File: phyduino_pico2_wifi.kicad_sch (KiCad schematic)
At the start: 14 parts, among them U11 ESP32-C6-MINI-1, U12 TS3A24159DRC

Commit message: nigthly commit
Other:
- company: (none) -> University of Toronto, Dept. of Physics
- title: (none) -> Phyduino Pico 2
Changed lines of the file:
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@@
 	(generator_version "10.0")
 	(paper "B")
+	(title_block
+		(title "Phyduino Pico 2")
+		(date "2026-05-04")
+		(rev "A")
+		(company "University of Toronto, Dept. of Physics")
+	)
 	(rectangle
 		(start 41.91 88.9)

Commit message: Made schematic changes : merged usb_pd sheet with wifi sheet. made system regulators adjustable.
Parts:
- removed C38: 0.1µF, Capacitor_SMD [KL]:C_0402_1005Metric, symbol Component - Device [KL]:C_Small
- removed TP16, TP17: TestPoint_Small, Component - Test point SMT [UL]:TestPoint_SameSky_CPG-47-TH-B, symbol Connector [KL]:TestPoint_Small
- removed U12: TS3A24159DRC, Package_SON [KL]:Texas_S-PVSON-N10, symbol Analog - Switches - Analog Devices [KL]:TS3A24159DRC
- added C131, C132: 0.1µF, Capacitor_SMD [KL]:C_0402_1005Metric, symbol Device:C_Small
- added C16, C24, C33, C35: 0.1μF, Capacitor_SMD [KL]:C_0805_2012Metric_Pad1.18x1.45mm_HandSolder, symbol Component - Device [KL]:C_Small
- added C17, C18, C25, C27, C36: 22µF, Capacitor_SMD [KL]:C_0805_2012Metric_Pad1.18x1.45mm_HandSolder, symbol Component - Device [KL]:C_Small
- added C19, C23, C29, C32: 10μF, Capacitor_SMD [KL]:C_0805_2012Metric_Pad1.18x1.45mm_HandSolder, symbol Component - Device [KL]:C_Small
- added C28, C9: 0.1µF, Capacitor_SMD [KL]:C_1206_3216Metric_Pad1.33x1.80mm_HandSolder, symbol Component - Device [KL]:C_Small
- added C30: 1µF, Capacitor_SMD [KL]:C_0402_1005Metric, symbol Component - Device [KL]:C_Small
- added C31, C6: 0.1µF, Capacitor_SMD [KL]:C_0402_1005Metric, symbol Component - Device [KL]:C_Small
- added C5, C7: 100pF, Capacitor_SMD [KL]:C_0805_2012Metric_Pad1.18x1.45mm_HandSolder, symbol Component - Device [KL]:C_Small
- added J6, J9: GT-USB-7047A, Connector - PC SMT [UL]:GCT-USBC-GCT_USB4110, symbol KL - Connector:USB_C_Receptacle_USB2.0_16P
- added L1: 6.8µH, Component - Inductor SMT [UL]:L_Bourns_SRP4021HMCT, symbol Inductor - Bourns:L_Bourns_SRP4021HMCT-3R3M
- added L2: 10µH, Component - Inductor SMT [UL]:L_Bourns_SRP4021HMCT, symbol Inductor - Bourns:L_Bourns_SRP4021HMCT-4R7M
- added Q1, Q2: SP30P25NQ, Package_DFN_QFN [KL]:Diodes_UDFN2020-6_Type-F, symbol UL - Transistors - MOSFET:PMPB27EP
- added R10: 5mΩ, Resistor_SMD [KL]:R_0603_1608Metric, symbol Component - Device [KL]:R_Small
- added R11, R12, R7, R8: 5.1kΩ, Resistor_SMD [KL]:R_0402_1005Metric, symbol Component - Device [KL]:R_Small
- added R134: 42.2kΩ, Resistor_SMD [KL]:R_0402_1005Metric, symbol Device:R_Small
- added R135, R138: 21kΩ, Resistor_SMD [KL]:R_0402_1005Metric, symbol Device:R_Small
- added R136, R137: 5.1kΩ, Resistor_SMD [KL]:R_0402_1005Metric, symbol Device:R_Small
- added R139, R141: 154kΩ, Resistor_SMD [KL]:R_0402_1005Metric, symbol Device:R_Small
- added R140, R143, R144: 39.2kΩ, Resistor_SMD [KL]:R_0402_1005Metric, symbol Device:R_Small
- added R142, R145: 10kΩ, Resistor_SMD [KL]:R_0402_1005Metric, symbol Device:R_Small
- added R37, R47, R48: 5.1kΩ, Resistor_SMD [KL]:R_0402_1005Metric, symbol phyduino_pico:R_Small
- added R40, R41: 100Ω, Resistor_SMD [KL]:R_0402_1005Metric, symbol phyduino_pico:R_Small
- added R51: 47kΩ, Resistor_SMD [KL]:R_0805_2012Metric_Pad1.20x1.40mm_HandSolder, symbol phyduino_pico:R_Small
- added R52: 16.5kΩ, Resistor_SMD [KL]:R_0805_2012Metric_Pad1.20x1.40mm_HandSolder, symbol phyduino_pico:R_Small
- added R53: 111kΩ, Resistor_SMD [KL]:R_0805_2012Metric_Pad1.20x1.40mm_HandSolder, symbol phyduino_pico:R_Small
- added R54: 18.7kΩ, Resistor_SMD [KL]:R_0805_2012Metric_Pad1.20x1.40mm_HandSolder, symbol phyduino_pico:R_Small
- added R56: 196kΩ, Resistor_SMD [KL]:R_0805_2012Metric_Pad1.20x1.40mm_HandSolder, symbol phyduino_pico:R_Small
- added R57: 62kΩ, Resistor_SMD [KL]:R_0805_2012Metric_Pad1.20x1.40mm_HandSolder, symbol phyduino_pico:R_Small
- added R58: 157kΩ, Resistor_SMD [KL]:R_0805_2012Metric_Pad1.20x1.40mm_HandSolder, symbol phyduino_pico:R_Small
- added R59: 30kΩ, Resistor_SMD [KL]:R_0805_2012Metric_Pad1.20x1.40mm_HandSolder, symbol phyduino_pico:R_Small
- added R6, R9: 220kΩ, Resistor_SMD [KL]:R_0805_2012Metric_Pad1.20x1.40mm_HandSolder, symbol Component - Device [KL]:R_Small
- added TH1: 10kΩ@25°C, Resistor_SMD [KL]:R_0402_1005Metric, symbol Component - Device [KL]:Thermistor_NTC
- added TP10, TP11, TP13, TP18, TP2, TP22, TP4, TP5, TP6, TP7: TestPoint_Small, Component - Test point SMT [UL]:TestPoint_SameSky_CPG-47-TH-B, symbol Connector [KL]:TestPoint_Small
- added U10, U8: AP63200WU, Package_TO_SOT_SMD [KL]:TSOT-23-6_HandSoldering, symbol Power - Switching Regulator [KL]:AP63200WU
- added U108, U109: TPS2121RUXR, Package - QFN [UL]:VQFN-HR-12, symbol PMIC - TI:TPS2121RUX
- added U6: AP33772SDKZ-13-FA02, Package_DFN_QFN [KL]:QFN-24-1EP_4x4mm_P0.5mm_EP2.75x2.75mm, symbol Interface - USB:AP33772S
- added U9: TPUSBLC6-2P6, Package_TO_SOT_SMD [KL]:SOT-666, symbol Protection - Signal:USBLC6-2P6
- added Z3: ESDA25P35-1U1M-ES, Diode_SMD [KL]:ST_QFN-2L_1.6x1.0mm, symbol phyduino_pico:D_Zener_Filled
- U11: value ESP32-C6-MINI-1 -> ESP32-C6-MINI-1-H4
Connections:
- net WIFI_UART_RX is gone; now on net WIFI_DL_UART_RX: TP9.1
- net WIFI_UART_TX is gone; now on net WIFI_DL_UART_TX: TP8.1
- net +3.3V: now also C17.1, C18.1, C5.1, L1.2, R56.1, R7.1, R8.1, U9.5 (VBUS)
- net GND: now also C131.2, C132.2, C17.2, C18.2, C19.2, C23.2, C25.2, C27.2, C28.2, C29.2, C30.1, C31.1, C32.2, C33.2, C35.2, C36.2, C6.1, C9.2, J6.A1 (GND), J6.A12 (GND), J6.B1 (GND), J6.B12 (GND), J9.A1 (GND), J9.A12 (GND), J9.B1 (GND), J9.B12 (GND), R11.2, R12.2, R134.1, R136.1, R137.1, R143.1, R144.1, R145.1, R47.2, R48.2, R52.2, R54.2, R57.2, R59.2, R6.2, R9.2, TH1.2, U10.4 (GND), U108.12 (GND), U108.3 (CP2), U108.6 (PR1), U108.9 (ST), U109.12 (GND), U6.25 (EP), U6.3 (GND), U8.4 (GND), U9.2 (GND), Z3.2 (A)
- net WIFI_AT_UART_CTS: now reaches U11.10 (IO5)
- net XTAL_32K_P: now reaches U11.12 (IO0)
- net XTAL_32K_N: now reaches U11.13 (IO1)
- net WIFI_AT_UART_RX: now reaches U11.15 (IO6)
- net WIFI_AT_UART_RX: now also R55.2
- net WIFI_AT_UART_TX: now reaches U11.16 (IO7)
- net WIFI_AT_UART_RTS: now reaches U11.9 (IO4)
- net AT_UART_RX: no longer names the net of U11.25 (IO19)
- net AT_UART_RX: no longer R55.2
- net AT_UART_TX: no longer names the net of U11.28 (IO22)
- net DL_UART_RX renamed WIFI_DL_UART_RX
- net DL_UART_TXD renamed WIFI_DL_UART_TX
- net WIFI_UART_CTS: no longer names the net of U11.20 (IO15)
- net WIFI_UART_RTS: no longer names the net of U11.19 (IO14)
- new net: J9.A6 (D+), J9.B6 (D+)
- new net: J9.A7 (D-), J9.B7 (D-)
- new net: R40.1, R41.2
- new net: U6.10 (NC), U6.14 (NC), U6.2 (NC), U6.21 (NC)
- new net +5.0V: U108.1 (OUT), U108.8 (OUT)
- new net +5.0V_DCDC: C25.1, C36.1, C7.1, L2.2, R135.2, R58.1, TP22.1, U108.7 (IN1)
- new net +VUSB: C19.1, C23.1, R138.2, R51.1, R53.1, TP13.1, U10.3 (IN), U108.2 (IN2), U109.1 (OUT), U109.8 (OUT), U8.3 (IN)
- new net +VUSB_COMM: C27.1, J6.A4 (VBUS), J6.A9 (VBUS), J6.B4 (VBUS), J6.B9 (VBUS), R139.2, TP18.1, U109.7 (IN1)
- new net +VUSB_PD: C29.1, C33.1, J9.A4 (VBUS), J9.A9 (VBUS), J9.B4 (VBUS), J9.B9 (VBUS), R10.1, U6.1 (ISENP), Z3.1 (K)
- new net +VUSB_PD_OUT: C32.1, C35.1, Q2.1 (D), Q2.2 (D), Q2.5 (D), Q2.6 (D), Q2.7 (D), R141.2, R41.1, TP11.1, U109.2 (IN2)
- new net DCDC_3V3_BST: C16.1, U8.6 (BST)
- new net DCDC_3V3_EN: R51.2, R52.1, U8.2 (EN)
- new net DCDC_3V3_FB: C5.2, R56.2, R57.1, U8.1 (FB)
- new net DCDC_3V3_SW: C16.2, L1.1, U8.5 (SW)
- new net DCDC_5V0_BST: C24.1, U10.6 (BST)
- new net DCDC_5V0_EN: R53.2, R54.1, U10.2 (EN)
- new net DCDC_5V0_FB: C7.2, R58.2, R59.1, U10.1 (FB)
- new net DCDC_5V0_SW: C24.2, L2.1, U10.5 (SW)
- new net I2C1_SCL: R7.2, U6.5 (SCL)
- new net I2C1_SDA: R8.2, U6.4 (SDA)
- new net PMUX_LIM: R134.2, U108.10 (ILM)
- new net PMUX_OV1: R135.1, R136.2, U108.5 (OV1)
- new net PMUX_OV2: R137.2, R138.1, U108.4 (OV2)
- new net PMUX_SS: C131.1, U108.11 (SS)
- new net PSW_STATUS: U109.9 (ST)
- new net USBPD_CC1: J9.A5 (CC1), R11.1, TP4.1, U6.17 (CC1)
- new net USBPD_CC2: J9.B5 (CC2), R12.1, TP6.1, U6.16 (CC2)
- new net USBPD_FLIP: U6.6 (FLIP)
- new net USBPD_GPIO: U6.7 (GPIO)
- new net USBPD_IFB: C31.2, U6.15 (IFB)
- new net USBPD_INT: U6.9 (INT)
- new net USBPD_OTP: TH1.1, U6.13 (OTP)
- new net USBPD_PROT_GATE: Q1.3 (G), Q2.3 (G), R37.1
- new net USBPD_PROT_SOURCE_DRAIN: Q1.4 (S), Q1.8 (S), Q2.4 (S), Q2.8 (S), TP5.1
- new net USBPD_PWR_EN: R37.2, TP10.1, U6.23 (PWR_EN)
- new net USBPD_V18: C6.2, U6.12 (V18)
- new net USBPD_V5V: C30.2, U6.20 (V5V)
- new net USBPD_VCC: Q1.1 (D), Q1.2 (D), Q1.5 (D), Q1.6 (D), Q1.7 (D), R10.2, TP2.1, U6.24 (VCC)
- new net USBPD_VOUT: R40.2, TP7.1, U6.22 (VOUT)
- new net USB_CC1: J6.A5 (CC1), R48.1
- new net USB_CC2: J6.B5 (CC2), R47.1
- new net USB_COM_D_N: J6.A7 (D-), J6.B7 (D-), U9.4 (I/O2)
- new net USB_COM_D_P: J6.A6 (D+), J6.B6 (D+), U9.6 (I/O1)
- new net USB_COM_SHIELD: C9.1, J6.S1 (SH), R6.1
- new net USB_D_N: U9.3 (I/O2)
- new net USB_D_P: U9.1 (I/O1)
- new net USB_PD_SHIELD: C28.1, J9.S1 (SH), R9.1
- new net USB_PMUX_CP2: R141.1, R142.2, U109.3 (CP2)
- new net USB_PMUX_LIM: R143.2, U109.10 (ILM)
- new net USB_PMUX_OV1: R140.1, R145.2, U109.5 (OV1)
- new net USB_PMUX_OV2: R142.1, R144.2, U109.4 (OV2)
- new net USB_PMUX_PR1: R139.1, R140.2, U109.6 (PR1)
- new net USB_PMUX_SS: C132.1, U109.11 (SS)
- no-connect marks 14 -> 28
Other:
- note added: "- 2.4GHz Wi-Fi 6 & BLE 5.0"
- note added: "- Both modules are pin compatiable, either can be used."
- note added: "- ESP-AT version 4.1.1.0"
- note added: "- ESP-AT version 5.0.1.0"
- note added: "- GitHub fork repo for ESP-AT: https://github.com/perc-sw/esp-at"
- note added: "- Hardware connection guide : https://docs.espressif.com/projects/esp-at/en/latest/esp32c6/Get_Started/Hardware_connection.html"
- note added: "- Hardware connection guide : https://docs.espressif.com/projects/esp-at/en/latest/esp32c61/Get_Started/Hardware_connection.html"
- note added: "- J6 Only provides +5.0V (3A) power and USB 2.0 communication."
- note added: "- J9 can negoiate +5.0V to 20.0V with current ouput varying form 100mA to 5.0A"
- note added: "- Not for low power applications."
- note added: "- To download ESP-AT firmware to ESP32 module use UART0 pins (TXD0 & RXD0)."
- note added: "- U10 will only enable when +VUSB is above +7.0V."
- note added: "- U108 select between +VUSB and the output of U10. If both voltages are below +5.5V, U10's output will be selected."
- note added: "- U109 will select which input power gets used. +VUSB_PD has priority if present."
- note added: "- U8 will only enable when +VUSB is above +4.3V."
- note added: "- Using ESP-AT as the network interface API."
- note added: ">1.06V"
- note added: "ESP32-C6-MINI-1:"
- note added: "ESP32-C61-MINI-1:"
- note added: "I^{2}C Addr = 0x52"
- note added: "I_{LIMIT} = 2.6A"
- note added: "I_{LIMIT} = 2.7A"
- note added: "Low=Disable, High=Enable"
- note added: "NOTES:"
- note added: "Over Voltage Protection = 22V"
- note added: "Over Voltage Protection= 5.5V"
- note added: "Required Hardware connections"
- note added: "System Power Regulators"
- note added: "UART/USB Firmware download"
- note added: "USB Power Delivery"
- note added: "V_{EN}=4.3V"
- note added: "V_{EN}=7.0V"
- note added: "V_{OVER} = 5.5V"
- note added: "WiFi Module Interface"
- moved on the sheet: C13, C37, R44, R45, R50, R55, TP14, TP8, TP9, U11

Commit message: development update.
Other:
- moved on the sheet: C132, R139, R140, R141, R142, R143, R144, R145, TP11, TP13, TP18, U109

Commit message: Made changes to the power tree to allow +Vin to power the board.
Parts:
- removed R53: 111kΩ, Resistor_SMD [KL]:R_0805_2012Metric_Pad1.20x1.40mm_HandSolder, symbol phyduino_pico:R_Small
- removed R54: 18.7kΩ, Resistor_SMD [KL]:R_0805_2012Metric_Pad1.20x1.40mm_HandSolder, symbol phyduino_pico:R_Small
- added C134: 0.1µF, Capacitor_SMD [KL]:C_0402_1005Metric, symbol Device:C_Small
- added R146, R149: 154kΩ, Resistor_SMD [KL]:R_0402_1005Metric, symbol Device:R_Small
- added R147: 49.2kΩ, Resistor_SMD [KL]:R_0402_1005Metric, symbol Device:R_Small
- added R150, R153: 10kΩ, Resistor_SMD [KL]:R_0402_1005Metric, symbol Device:R_Small
- added R151, R152: 39.2kΩ, Resistor_SMD [KL]:R_0402_1005Metric, symbol Device:R_Small
- added TP16, TP17: TestPoint_Small, Component - Test point SMT [UL]:TestPoint_SameSky_CPG-47-TH-B, symbol Connector [KL]:TestPoint_Small
- added U110: TPS2121RUXR, Package - QFN [UL]:VQFN-HR-12, symbol PMIC - TI:TPS2121RUX
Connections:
- net PSW_STATUS is gone; now on net GND: U109.9 (ST)
- net +3.3V: now also R153.2
- net +VUSB_COMM: now also TP16.1, U110.2 (IN2); no longer TP18.1, U109.7 (IN1)
- net +VUSB_PD_OUT: now also TP18.1, U109.7 (IN1), R149.2; no longer R141.2, TP11.1, U109.2 (IN2)
- net DCDC_5V0_EN: now also U108.9 (ST), R153.1
- net GND: now also C134.2, R147.1, R151.1, R152.1, U110.12 (GND), U110.5 (OV1), U110.9 (ST); no longer U108.9 (ST)
- net +VUSB renamed +VMUX
- net +VMUX: now also TP17.1, U110.1 (OUT), U110.8 (OUT); no longer TP13.1, U109.1 (OUT), U109.8 (OUT)
- net USB_PMUX_CP2 renamed USB_PMUX1_CP2
- net USB_PMUX_LIM renamed USB_PMUX1_LIM
- net USB_PMUX_OV1 renamed USB_PMUX2_OV2
- net USB_PMUX2_OV2: now also U110.4 (OV2); no longer U109.5 (OV1)
- net USB_PMUX_OV2 renamed USB_PMUX1_OV2
- net USB_PMUX_PR1 renamed USB_PMUX2_CP2
- net USB_PMUX2_CP2: now also U110.3 (CP2); no longer U109.6 (PR1)
- net USB_PMUX_SS renamed USB_PMUX1_SS
- new net +VIN: R141.2, TP11.1, U109.2 (IN2)
- new net +VUSB_IN: R146.2, TP13.1, U109.1 (OUT), U109.8 (OUT), U110.7 (IN1)
- new net USB_PMUX1_OV1: R150.1, R151.2, U109.5 (OV1)
- new net USB_PMUX1_PR1: R149.1, R150.2, U109.6 (PR1)
- new net USB_PMUX2_LIM: R152.2, U110.10 (ILM)
- new net USB_PMUX2_PR1: R146.1, R147.2, U110.6 (PR1)
- new net USB_PMUX2_SS: C134.1, U110.11 (SS)
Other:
- note added: "- +VIN input can vary between +9.0V and +20.0V"
- note added: "Enables +5.0V DC/DC when VIN2 > 6.0V"
- note added: "ST [0b1] = IN1 ST [0b0] = IN2"
- note removed: "Over Voltage Protection = 22V"
- note removed: "Over Voltage Protection= 5.5V"
- note removed: "V_{EN}=7.0V"
- moved on the sheet: C131, C132, C16, C17, C18, C19, C23, C24, C25, C27, C28, C29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

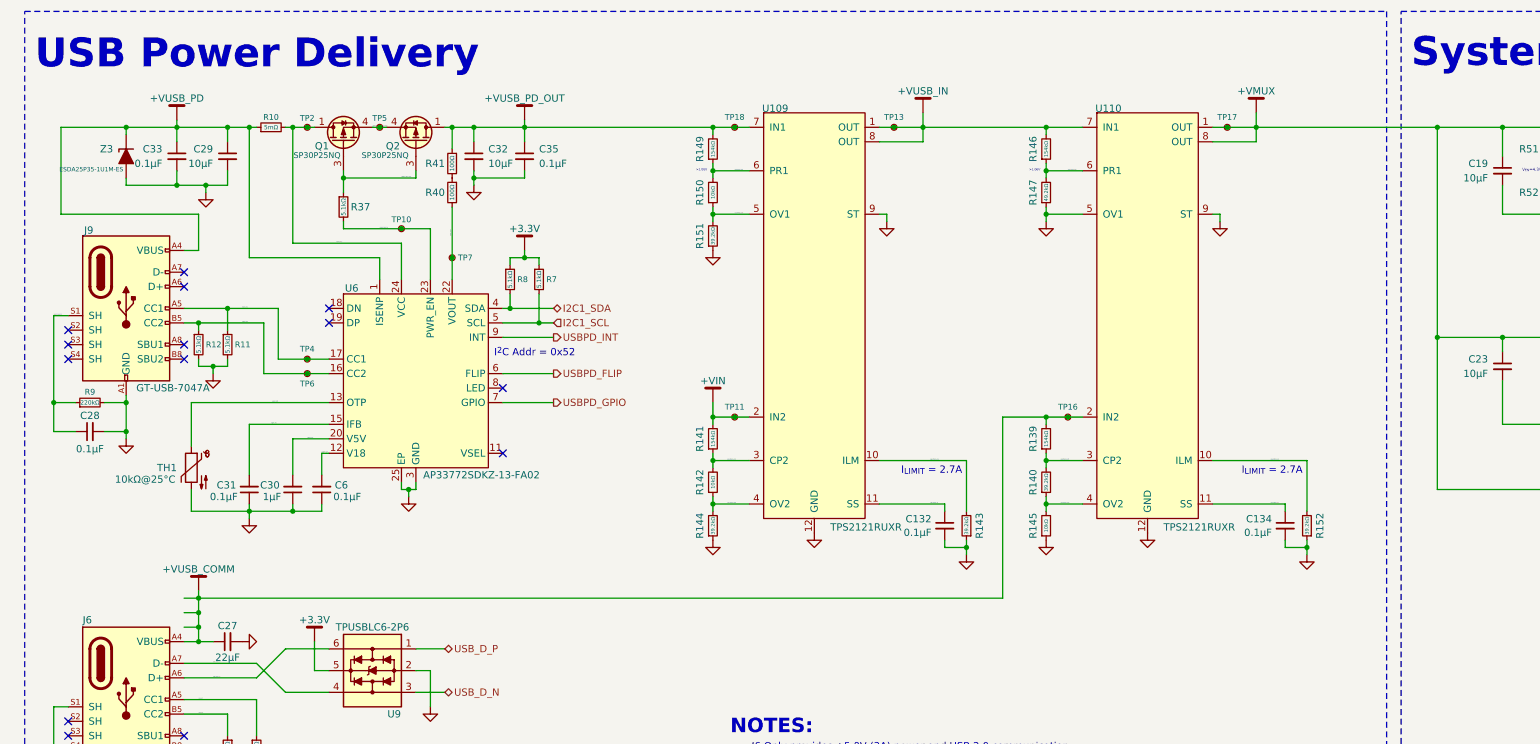
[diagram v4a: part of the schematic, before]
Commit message: Changed power tree to accept +Vin.
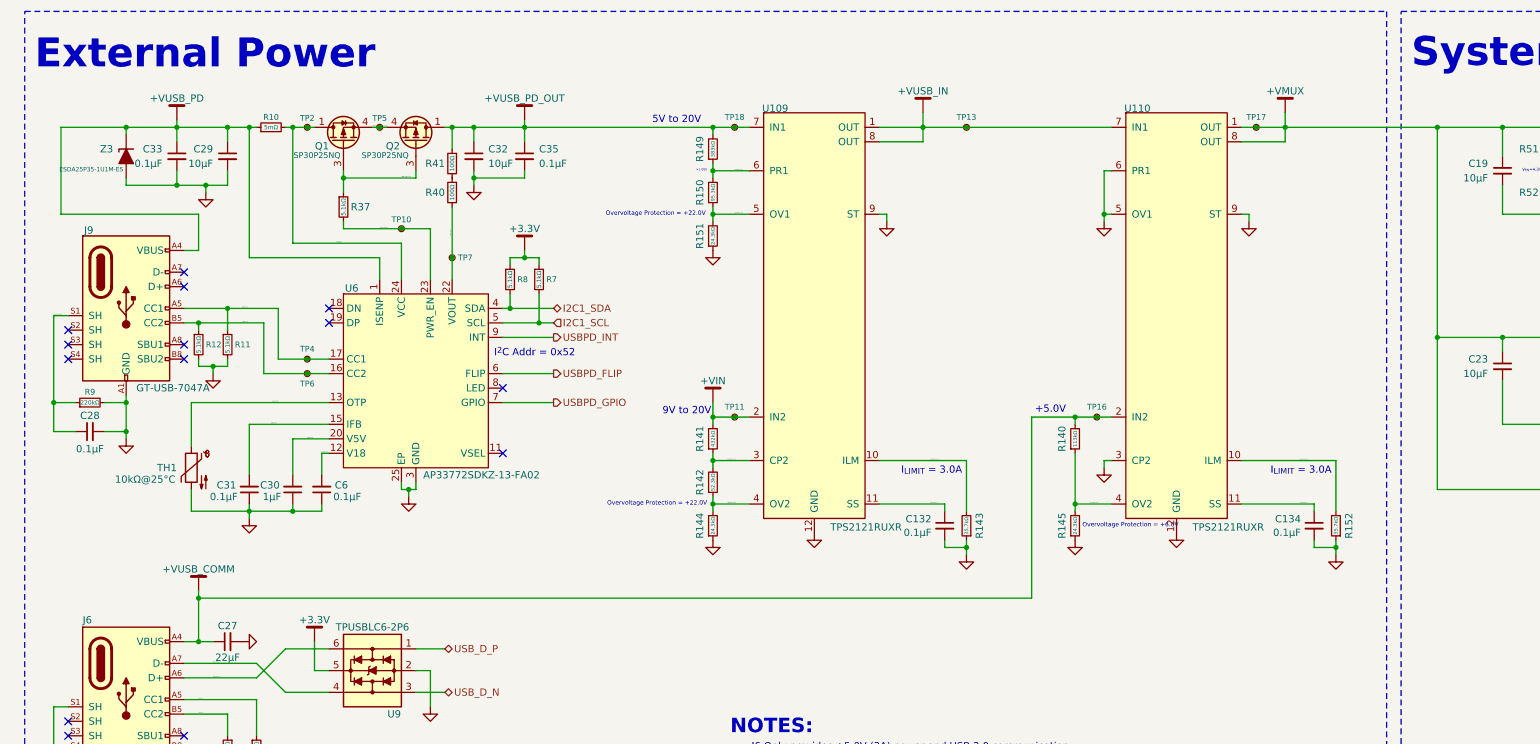
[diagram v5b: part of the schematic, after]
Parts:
- removed R139, R146: 154kΩ, Resistor_SMD [KL]:R_0402_1005Metric, symbol Device:R_Small
- removed R147: 49.2kΩ, Resistor_SMD [KL]:R_0402_1005Metric, symbol Device:R_Small
- R140: value 39.2kΩ -> 113kΩ
- R141: value 154kΩ -> 432kΩ
- R142: value 10kΩ -> 52.3kΩ
- R143, R152: value 39.2kΩ -> 35.7kΩ
- R144, R151: value 39.2kΩ -> 24.3kΩ
- R145: value 10kΩ -> 24.3kΩ
- R149: value 154kΩ -> 383kΩ
- R150: value 10kΩ -> 95.3kΩ
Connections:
- net USB_PMUX2_PR1 is gone; now on net GND: U110.6 (PR1)
- net +VUSB_COMM: now also R140.2
- net GND: now also U110.3 (CP2)
- removed net USB_PMUX2_CP2: R140.2, U110.3 (CP2)
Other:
- note added: "+5.0V"
- note added: "5V to 20V"
- note added: "9V to 20V"
- note added: "External Power"
- note added: "I_{LIMIT} = 3.0A"
- note added: "Overvoltage Protection = +22.0V"
- note added: "Overvoltage Protection = +6.0V"
- note removed: "I_{LIMIT} = 2.7A"
- note removed: "USB Power Delivery"
- moved on the sheet: C134, R140, R145, R152, TP13, TP16, TP17, U110
